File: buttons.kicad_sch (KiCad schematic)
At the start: 4 parts, among them SW1 SW_Push, SW2 SW_Push, SW3 SW_Push, SW4 SW_Push

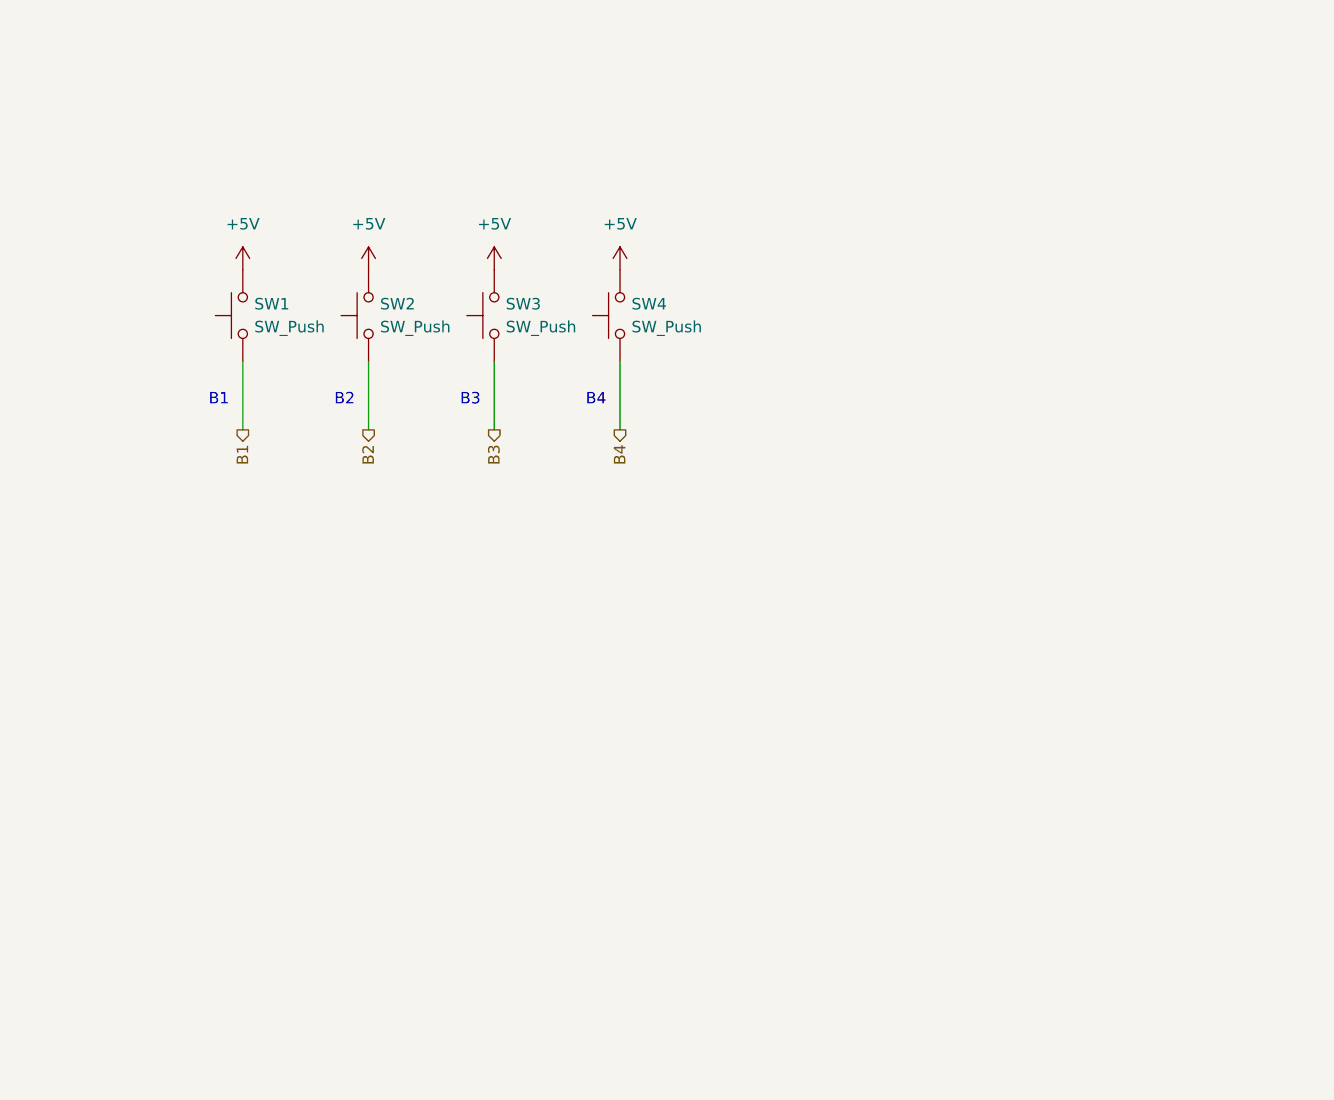
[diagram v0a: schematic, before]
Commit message: Added Gesture sensor and Audio system schematics and properly fixed port directions
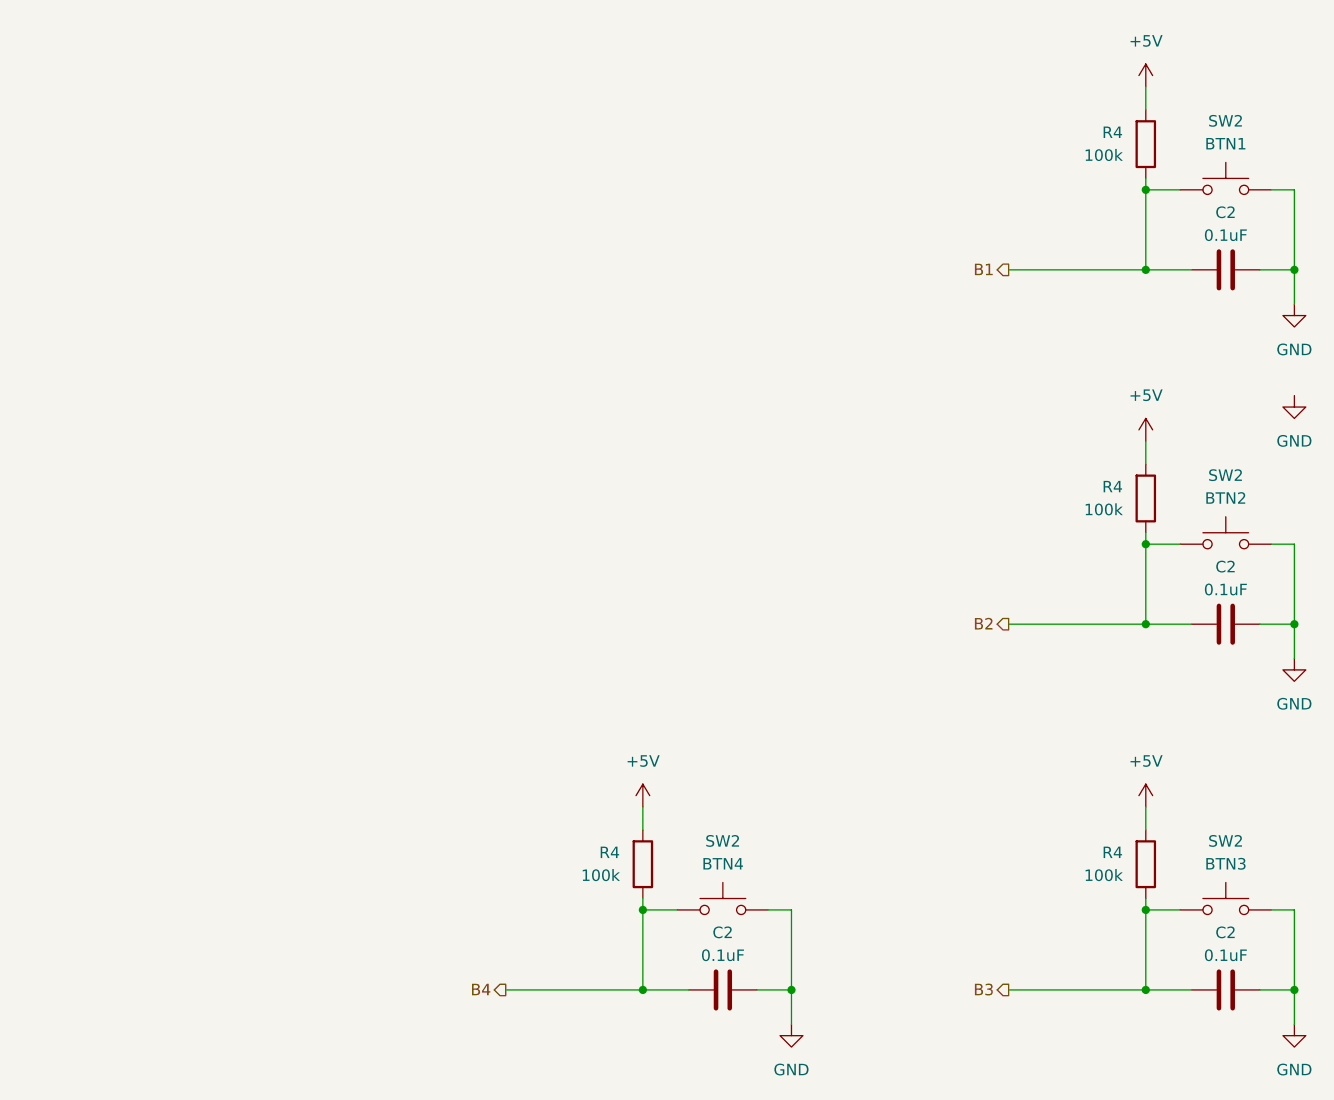
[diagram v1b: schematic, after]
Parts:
- removed SW1, SW2, SW3, SW4: SW_Push, symbol Switch:SW_Push
- added C2 (x4): 0.1uF, symbol Device:C
- added R4 (x4): 100k, symbol Device:R
- added SW2: BTN4, symbol Switch:SW_Push
- added SW2: BTN1, symbol Switch:SW_Push
- added SW2: BTN3, symbol Switch:SW_Push
- added SW2: BTN2, symbol Switch:SW_Push
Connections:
- net +5V: now also R4.2, R4.2, R4.2, R4.2
- net B1: now also C2.2, R4.1, SW2.2
- net B2: now also C2.2, R4.1, SW2.2
- net B3: now also C2.2, R4.1, SW2.2
- net B4: now also C2.2, R4.1, SW2.2
- new net GND: C2.1, C2.1, C2.1, C2.1, SW2.1, SW2.1, SW2.1, SW2.1
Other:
- note removed: "B1"
- note removed: "B2"
- note removed: "B3"
- note removed: "B4"

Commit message: Finalized Schematic
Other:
- moved on the sheet: C2, R4, SW2
